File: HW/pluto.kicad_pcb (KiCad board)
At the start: 4 copper layers, 99.8 x 99.8 mm, 66 parts, among them J1 VCC1, J10 GND3, J11 Expansion Bus, J12 VIA2PB, J2 GND1, J3 VCC2, J4 POWER, J5 GND2, J6 RS232a, J7 RS232b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

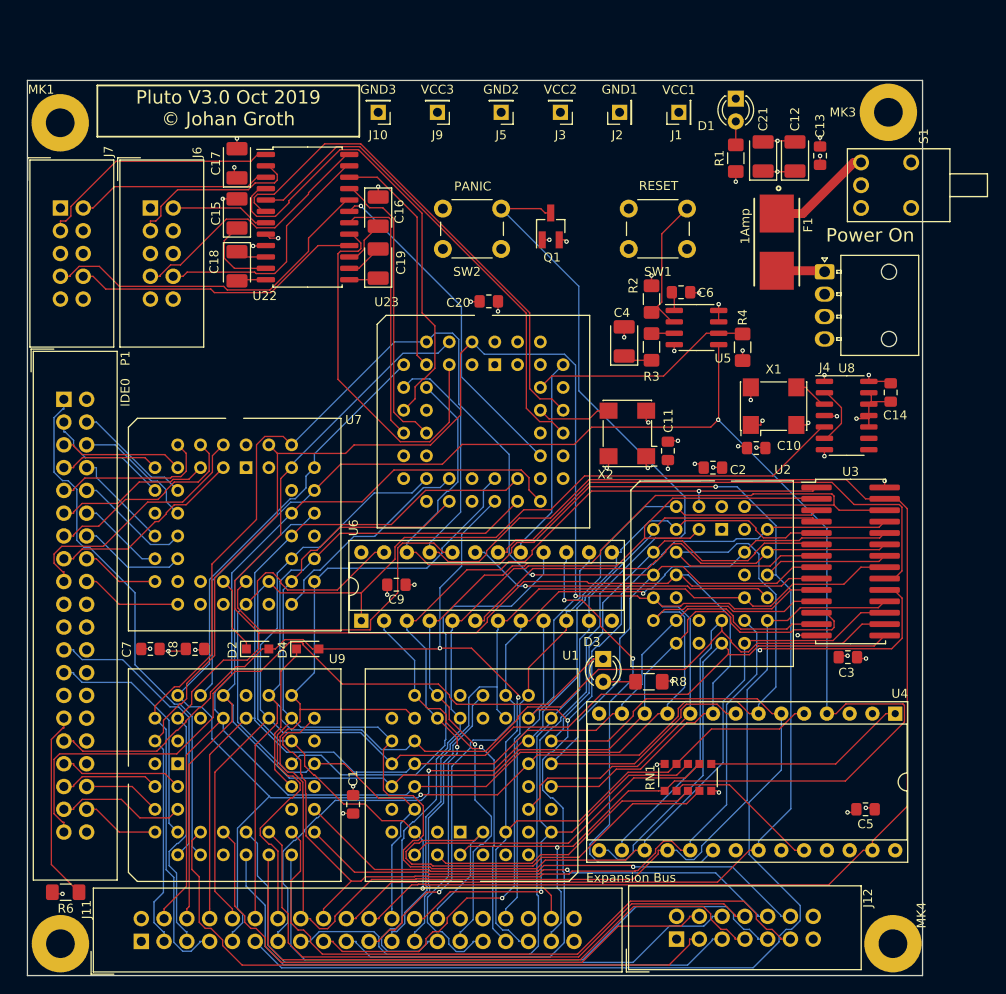
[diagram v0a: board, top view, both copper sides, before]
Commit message: New version with a TL16C550 UART
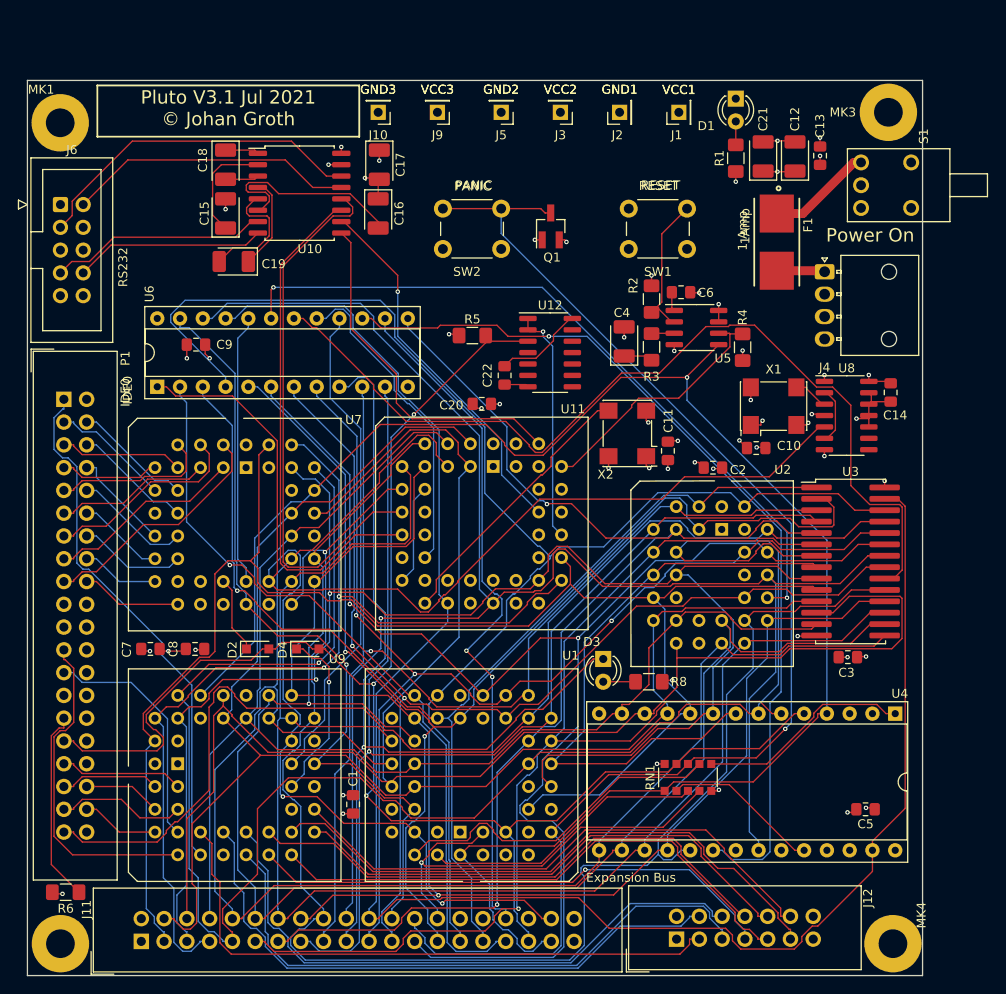
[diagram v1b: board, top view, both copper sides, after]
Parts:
- removed J7: RS232b, Connector_IDC:IDC-Header_2x05_P2.54mm_Vertical
- removed U22: MAX238, Package_SO:SOIC-24W_7.5x15.4mm_P1.27mm
- removed U23: SC28L92PLCC44, Package_LCC:PLCC-44_THT-Socket
- added C22: 0.1uF, Capacitor_SMD:C_0805_2012Metric_Pad1.15x1.40mm_HandSolder, F.Cu at (108.0, 73.0)
- added R5: 3.3k, Resistor_SMD:R_1206_3216Metric_Pad1.42x1.75mm_HandSolder, F.Cu at (104.4, 68.6)
- added U10: MAX232, Package_SO:SOIC-16W_7.5x10.3mm_P1.27mm, F.Cu at (85.1, 52.7)
- added U11: ST16C550PLCC44, Package_LCC:PLCC-44_THT-Socket, F.Cu at (106.7, 83.2)
- added U12: 74LS03, Package_SO:SOIC-14_3.9x8.7mm_P1.27mm, F.Cu at (113.0, 70.5)
- moved C9 34.9 mm to (73.5, 69.6)
- moved U6 34.6 mm to (69.2, 74.3)
- moved C19 16.1 mm to (77.8, 60.3), turned to 180 degrees
- moved C17 15.9 mm to (94.0, 49.5), turned to 270 degrees
- moved C20 11.5 mm to (105.4, 76.2)
- moved C18 11.4 mm to (76.8, 49.5)
- moved J6 10.0 mm to (58.4, 54.0)
- moved C15 1.27 mm to (76.8, 55.0)
- moved C16 0.20 mm to (93.9, 55.0)
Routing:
- net GND: track 128.5 -> 39.7 mm, vias 25 -> 24
- net VCC: track 125.2 -> 42.5 mm, vias 30 -> 31
- net /Address decoding and support section/A11: track 90.8 -> 159.2 mm, vias 0 -> 2
- net /DUART and RS232/RX: track 0.00 -> 61.6 mm
- net /DUART and RS232/TX: track 0.00 -> 58.1 mm
- net Net-(U22-Pad6): track 56.5 -> 0.00 mm
- net /Address decoding and support section/A13: track 108.5 -> 163.7 mm, vias 1 -> 0
- net Net-(U22-Pad5): track 55.0 -> 0.00 mm
- net Net-(U22-Pad4): track 53.1 -> 0.00 mm
- net /Address decoding and support section/~ROMSEL: track 34.7 -> 81.7 mm, vias 1 -> 2
- net /Address decoding and support section/~RTC: track 54.7 -> 100.2 mm, vias 2 -> 1
- net /Address decoding and support section/~RAMSEL: track 59.1 -> 103.3 mm
- net /Address decoding and support section/A5: track 96.4 -> 140.3 mm, vias 1 -> 2
- net /Address decoding and support section/A15: track 43.1 -> 85.7 mm
- net /DUART and RS232/CTSb: track 41.7 -> 0.00 mm
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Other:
- board text added: "1 Amp"
- board text added: "GND1"
- board text added: "GND2"
- board text added: "GND3"
- board text added: "IDE0"
- board text added: "PANIC"
- board text added: "Pluto V3.1 Jul 2021 © Johan Groth"
- board text added: "RESET"
- board text added: "RS232"
- board text added: "VCC1"
- board text added: "VCC2"
- board text added: "VCC3"
- board text removed: "Pluto V3.0 Oct 2019 © Johan Groth"

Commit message: small updates
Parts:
- moved SW2 7.22 mm to (102.0, 54.4), turned to 0 degrees
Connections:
- net Net-(U11-Pad18) renamed /DUART and RS232/UART_CLK
- C22 pad 1: Net-(C22-Pad1) -> GND
- C22 pad 2: Net-(C22-Pad2) -> VCC
- Q1 pad 1: GND -> /Address decoding and support section/~NMI
- Q1 pad 3: /Address decoding and support section/~NMI -> GND
- U12 pad 14: Net-(C22-Pad2) -> VCC
- U12 pad 7: Net-(C22-Pad1) -> GND
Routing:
- net /Address decoding and support section/~NMI: track 147.3 -> 87.3 mm, vias 1 -> 2
- net VCC: track 42.5 -> 52.6 mm
- net Net-(C22-Pad2): track 10.1 -> 0.00 mm
- net Net-(C22-Pad1): track 2.71 -> 0.00 mm
- net GND: track 39.7 -> 41.6 mm, vias 24 -> 23
